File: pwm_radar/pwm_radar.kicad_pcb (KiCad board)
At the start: 2 copper layers, 32.6 x 46.1 mm, 21 parts, among them J1 Conn_Coaxial, J2 Conn_01x01_Pin, J3 Conn_01x01_Pin, J4 Conn_Coaxial, J5 Conn_Coaxial, J6 Conn_Coaxial, J7 Conn_01x01_Pin, J8 Conn_01x01_Pin

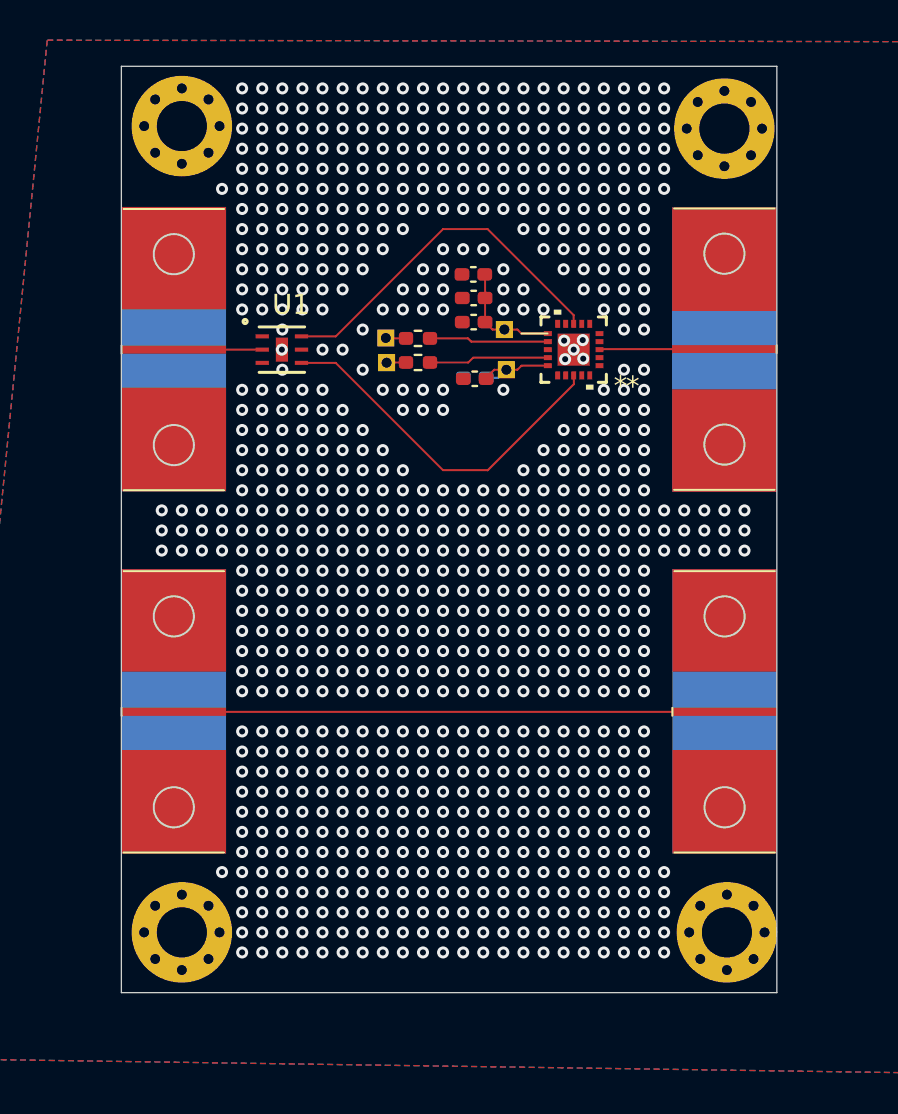
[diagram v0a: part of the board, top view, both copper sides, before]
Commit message: added 50 ohm lines
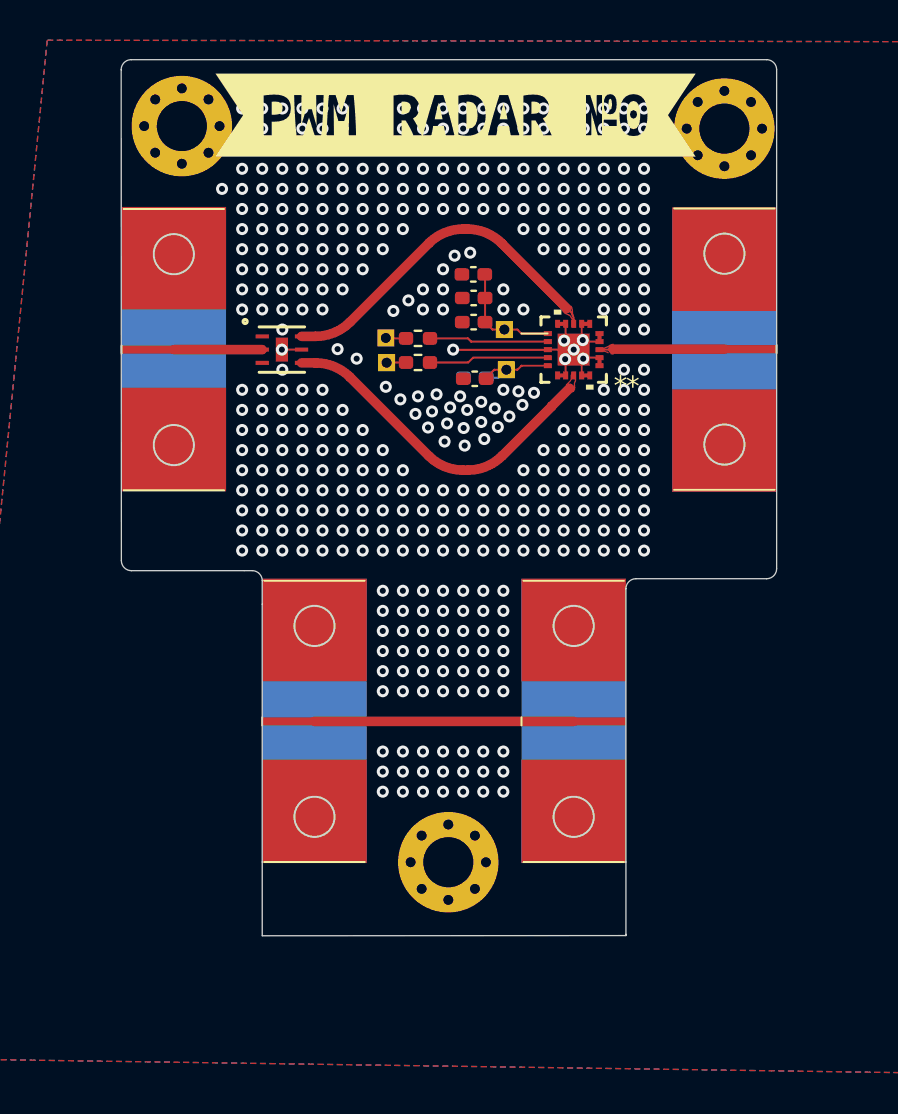
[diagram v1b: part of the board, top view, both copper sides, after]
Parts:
- removed H3: MountingHole_Pad, MountingHole:MountingHole_2.5mm_Pad_Via
- added kibuzzard-6A209544: G***, kibuzzard-6A209544, F.Cu at (126.6, 86.3)
- added kibuzzard-6A209595: G***, kibuzzard-6A209595, B.Cu at (126.4, 86.5)
- moved J5 20.4 mm to (113.1, 116.5)
- moved J4 19.9 mm to (126.0, 116.5)
- moved H4 13.7 mm to (126.3, 123.5)
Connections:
- U2 pad 21: (no net) -> GND
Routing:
- net Net-(J4-In): track 27.4 -> 12.9 mm
- net GND: track 0.00 -> 14.1 mm, vias 825 -> 464
- net RF2: track 18.0 -> 16.9 mm
- net (no net): vias 7 -> 2
- added copper zone on F.Cu, net Net-(J6-In)
- added copper zone on F.Cu, net RF1
- added copper zone on F.Cu, net RF2
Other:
- board size 32.6 x 46.1 mm -> 32.6 x 43.6 mm

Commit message: minor changes
minor changes
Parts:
- moved J4 13.0 mm to (139.0, 116.5), turned to -90 degrees
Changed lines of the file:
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@@
 	(footprint "pwm_radar_lib:Wurth_RF_PWM_Conn"
 		(layer "F.Cu")
-		(at 126 116.5 90)
+		(at 139.005845 116.5 -90)
 		(property "Reference" "J4"
-			(at -9.9 4 90)
+			(at -9.9 4 270)
 			(unlocked yes)
 			(layer "F.SilkS")
@@
 		)
 		(property "Value" "Conn_Coaxial"
-			(at 0 1 90)
+			(at 0 1 270)
 			(unlocked yes)
 			(layer "F.Fab")
@@
 		)
 		(property "Datasheet" ""
-			(at 0 0 90)
+			(at 0 0 270)
 			(unlocked yes)
 			(layer "F.Fab")
@@
 		)
 		(property "Description" "coaxial connector (BNC, SMA, SMB, SMC, Cinch/RCA, LEMO, ...)"
-			(at 0 0 90)
+			(at 0 0 270)
 			(unlocked yes)
 			(layer "F.Fab")
@@
 		(attr smd)
 		(fp_line
-			(start -0.2 3.9)
-			(end 0.2 3.9)
+			(start -7 9)
+			(end -7 4)
 			(stroke
 				(width 0.1)
@@
 		)
 		(fp_line
-			(start -7 9)
-			(end -7 4)
+			(start -0.2 3.9)
+			(end 0.2 3.9)
 			(stroke
 				(width 0.1)
@@
 		)
 		(fp_circle
-			(center 4.75 6.5)
-			(end 4.75 7.5)
+			(center -4.75 6.5)
+			(end -4.75 7.5)
 			(stroke
 				(width 0.1)
@@
 		)
 		(fp_circle
-			(center -4.75 6.5)
-			(end -4.75 7.5)
+			(center 4.75 6.5)
+			(end 4.75 7.5)
 			(stroke
 				(width 0.1)
@@
 		)
 		(fp_text user "${REFERENCE}"
-			(at 0 2.5 90)
+			(at 0 2.5 270)
 			(unlocked yes)
 			(layer "F.Fab")
@@
 		)
 		(pad "1" connect rect
-			(at 0 6.5 90)
+			(at 0 6.5 270)
 			(size 0.4 5.2)
 			(layers "F.Cu" "F.Mask")
@@
 		)
 		(pad "2" connect rect
-			(at -4.475 6.5 90)
+			(at -4.475 6.5 270)
 			(size 5.15 5.2)
 			(layers "F.Cu" "F.Mask")
@@
 		)
 		(pad "2" connect rect
-			(at 0.025 6.5 90)
+			(at 0.025 6.5 270)
 			(size 14.15 5.2)
 			(layers "B.Cu" "B.Mask")
@@
 		)
 		(pad "2" connect rect
-			(at 4.55 6.5 90)
+			(at 4.55 6.5 270)
 			(size 5.1 5.2)
 			(layers "F.Cu" "F.Mask")
@@
 		)
 	)
+	(gr_poly
+		(pts
+			(xy 136.55 98.2) (xy 136.55 97.73) (xy 134.49 97.74) (xy 133.96 97.92) (xy 133.96 98.08) (xy 134.44 98.2)
+		)
+		(stroke
+			(width 0.1)
+			(type solid)
+		)
+		(fill yes)
+		(layer "F.Mask")
+	)
 	(gr_rect
 		(start 110 83.695)
@@
 	)
 	(gr_rect
+		(start 110 109.025)
+		(end 142.61 130.305)
+		(stroke
+			(width 0.1)
+			(type solid)
+		)
+		(fill yes)
+		(layer "F.Mask")
+	)
+	(gr_rect
+		(start 110 123)
+		(end 142.61 130.255)
+		(stroke
+			(width 0.1)
+			(type solid)
+		)
+		(fill yes)
+		(layer "F.Mask")
+	)
+	(gr_rect
 		(start 110.1 105)
 		(end 142.51 109.025)
@@
 		(layer "F.Mask")
 	)
+	(gr_line
+		(start 133.96 97.92)
+		(end 133.96 98.08)
+		(stroke
+			(width 0.1)
+			(type default)
+		)
+		(layer "F.Mask")
+	)
+	(gr_line
+		(start 133.96 98.08)
+		(end 134.44 98.2)
+		(stroke
+			(width 0.1)
+			(type default)
+		)
+		(layer "F.Mask")
+	)
+	(gr_line
+		(start 134.44 98.2)
+		(end 136.55 98.2)
+		(stroke
+			(width 0.1)
+			(type default)
+		)
+		(layer "F.Mask")
+	)
+	(gr_line
+		(start 134.49 97.74)
+		(end 133.96 97.92)
+		(stroke
+			(width 0.1)
+			(type default)
+		)
+		(layer "F.Mask")
+	)
+	(gr_line
+		(start 136.55 97.73)
+		(end 134.49 97.74)
+		(stroke
+			(width 0.1)
+			(type default)
+		)
+		(layer "F.Mask")
+	)
+	(gr_line
+		(start 136.55 98.2)
+		(end 136.55 97.73)
+		(stroke
+			(width 0.1)
+			(type default)
+		)
+		(layer "F.Mask")
+	)
 	(gr_rect
 		(start 136.61 83.645)
@@
 	)
 	(gr_rect
-		(start 109.995 124)
-		(end 142.605 130)
+		(start 110 109)
+		(end 142.61 130.255)
+		(stroke
+			(width 0.1)
+			(type solid)
+		)
+		(fill yes)
+		(layer "B.Mask")
+	)
+	(gr_rect
+		(start 110 123.255)
+		(end 142.61 130.255)
 		(stroke
 			(width 0.1)
@@
 	(gr_rect
 		(start 110.1 105)
-		(end 142.51 109.025)
+		(end 142.51 110.025)
 		(stroke
 			(width 0.1)
@@
 		(layer "B.Mask")
 	)
+	(gr_rect
+		(start 110.1 109.025)
+		(end 142.61 130.255)
+		(stroke
+			(width 0.1)
+			(type solid)
+		)
+		(fill no)
+		(layer "B.Mask")
+	)

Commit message: pcb files changes
pcb changes
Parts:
- added H3: MountingHole_Pad, MountingHole:MountingHole_2.5mm_Pad_Via, F.Cu at (138.4, 127.3)
- moved H4 12.4 mm to (114.4, 126.9)
- moved J4 6.24 mm to (145.2, 116.5)
- moved J5 5.75 mm to (107.3, 116.5)
- moved H2 0.64 mm to (139.6, 86.5)
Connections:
- U2 pad 21: GND -> (no net)
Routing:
- net Net-(J4-In): track 12.9 -> 24.9 mm
- net GND: vias 464 -> 554
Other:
- board size 32.6 x 43.6 mm -> 32.6 x 47.3 mm

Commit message: changes
changes
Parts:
- removed J1, J4, J5: Conn_Coaxial, pwm_radar_lib:Wurth_RF_PWM_Conn
- removed kibuzzard-6A209544: G***, kibuzzard-6A209544
- removed kibuzzard-6A209595: G***, kibuzzard-6A209595
- added C6: 100p, Capacitor_SMD:C_0402_1005Metric_Pad0.74x0.62mm_HandSolder, F.Cu at (199.0, 65.3)
- C4, J2, J3, J7, J8: moved to F.Cu
- moved U1 107.7 mm to (211.6, 44.7)
- moved H4 100.8 mm to (194.1, 65.2)
- moved U2 99.5 mm to (216.4, 44.7)
- moved J2 92.9 mm to (199.1, 43.8), turned to 0 degrees
- moved H1 91.1 mm to (194.1, 45.5)
- moved J7 90.2 mm to (199.1, 49.9), turned to 0 degrees
- moved H3 88.5 mm to (194.1, 58.6)
- moved R1 88.2 mm to (202.3, 55.5), turned to 0 degrees
- moved R2 87.8 mm to (202.3, 57.5), turned to 0 degrees
- moved J6 87.4 mm to (223.0, 55.7)
- moved J3 86.1 mm to (199.1, 46.9), turned to 0 degrees
- moved J8 83.7 mm to (199.1, 53.0), turned to 0 degrees
- moved C1 82.5 mm to (199.0, 55.5), turned to 0 degrees
- moved C2 81.0 mm to (199.0, 57.4), turned to 0 degrees
- moved C4 80.9 mm to (199.0, 61.4), turned to 0 degrees
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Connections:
- J6 pad 1: Net-(J6-In) -> (no net)
- J6 pad 2: GND -> (no net)
- U1 pad 1: GND -> (no net)
- U1 pad 2: Net-(J1-In) -> (no net)
- U1 pad 3: GND -> (no net)
- U1 pad 4: RF2 -> (no net)
- U1 pad 5: GND -> (no net)
- U1 pad 6: RF1 -> (no net)
- U1 pad 7: GND -> (no net)
- U2 pad 1: GND -> (no net)
- U2 pad 10: GND -> (no net)
- U2 pad 11: VDD -> (no net)
- U2 pad 12: CTRL -> (no net)
- U2 pad 13: GND -> (no net)
- U2 pad 14: EN -> (no net)
- U2 pad 15: VSS -> (no net)
- U2 pad 16: GND -> (no net)
- U2 pad 17: GND -> (no net)
- U2 pad 18: RF2 -> (no net)
- U2 pad 19: GND -> (no net)
- U2 pad 2: GND -> (no net)
- U2 pad 20: GND -> (no net)
- U2 pad 3: Net-(J6-In) -> (no net)
- U2 pad 4: GND -> (no net)
- U2 pad 5: GND -> (no net)
- U2 pad 6: GND -> (no net)
- U2 pad 7: GND -> (no net)
- U2 pad 8: RF1 -> (no net)
- U2 pad 9: GND -> (no net)
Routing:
- net Net-(J4-In): track 24.9 -> 0.00 mm
- net RF1: track 17.6 -> 0.00 mm
- net RF2: track 16.9 -> 0.00 mm
- net GND: track 14.1 -> 0.00 mm, vias 554 -> 0
- net Net-(J6-In): track 6.26 -> 0.00 mm
- net EN: track 5.96 -> 0.00 mm
- net CTRL: track 5.93 -> 0.00 mm
- net VDD: track 5.74 -> 0.00 mm
- net VSS: track 4.53 -> 0.00 mm
- net Net-(J1-In): track 4.40 -> 0.00 mm
- net Net-(J7-Pin_1): track 1.02 -> 0.00 mm
- net Net-(J2-Pin_1): track 1.00 -> 0.00 mm
- net (no net): vias 2 -> 0
- removed copper zone on B.Cu, net GND
- removed copper zone on F.Cu, net GND
- removed copper zone on F.Cu, net Net-(J6-In)
- removed copper zone on F.Cu, net RF1
- removed copper zone on F.Cu, net RF2
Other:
- board size 32.6 x 47.3 mm -> 2 x 11.5 mm

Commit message: pcb changes
pcb changes
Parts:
- added J1: Conn_Coaxial, pwm_radar_lib:Wurth_RF_PWM_Conn, F.Cu at (83.6, 57.0)
- added J4: Conn_Coaxial, pwm_radar_lib:Wurth_RF_PWM_Conn, F.Cu at (130.0, 76.0)
- added J5: Conn_Coaxial, pwm_radar_lib:Wurth_RF_PWM_Conn, F.Cu at (83.0, 76.0)
- C1, C2, C3, C4, C5, C6, J2, J3, J7, J8: moved to B.Cu
- moved U1 114.3 mm to (98.0, 57.0)
- moved J6 106.5 mm to (116.5, 57.0), turned to 90 degrees
- moved U2 103.2 mm to (114.0, 57.0)
- moved J2 95.0 mm to (104.9, 56.7), turned to 180 degrees
- moved R1 94.9 mm to (107.4, 56.6), turned to 180 degrees
- moved R2 92.1 mm to (110.1, 57.8), turned to 180 degrees
- moved J7 92.1 mm to (107.4, 58.4), turned to 180 degrees
- moved C4 91.6 mm to (107.4, 60.0), turned to 180 degrees
- moved C6 91.6 mm to (107.5, 62.4), turned to 180 degrees
- moved C5 91.6 mm to (107.5, 61.2), turned to 180 degrees
- moved C3 91.1 mm to (108.0, 55.7), turned to 180 degrees
- moved C2 91.1 mm to (108.0, 54.6), turned to 180 degrees
- moved C1 91.0 mm to (108.0, 53.5), turned to 180 degrees
- moved J3 89.6 mm to (109.9, 55.6), turned to 180 degrees
- moved J8 89.5 mm to (109.8, 60.0), turned to 180 degrees
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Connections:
- J6 pad 1: (no net) -> Net-(J6-In)
- J6 pad 2: (no net) -> GND
- U1 pad 1: (no net) -> GND
- U1 pad 2: (no net) -> Net-(J1-In)
- U1 pad 3: (no net) -> GND
- U1 pad 4: (no net) -> RF1-
- U1 pad 5: (no net) -> GND
- U1 pad 6: (no net) -> RF1+
- U1 pad 7: (no net) -> GND
- U2 pad 1: (no net) -> GND
- U2 pad 10: (no net) -> GND
- U2 pad 11: (no net) -> VDD
- U2 pad 12: (no net) -> CTRL
- U2 pad 13: (no net) -> GND
- U2 pad 14: (no net) -> EN
- U2 pad 15: (no net) -> VSS
- U2 pad 16: (no net) -> GND
- U2 pad 17: (no net) -> GND
- U2 pad 18: (no net) -> RF1-
- U2 pad 19: (no net) -> GND
- U2 pad 2: (no net) -> GND
- U2 pad 20: (no net) -> GND
- U2 pad 21: (no net) -> GND
- U2 pad 3: (no net) -> Net-(J6-In)
- U2 pad 4: (no net) -> GND
- U2 pad 5: (no net) -> GND
- U2 pad 6: (no net) -> GND
- U2 pad 7: (no net) -> GND
- U2 pad 8: (no net) -> RF1+
- U2 pad 9: (no net) -> GND
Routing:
- net Net-(J4-In): track 0.00 -> 38.0 mm
- net RF1+: track 0.00 -> 19.8 mm
- net RF1-: track 0.00 -> 19.8 mm
- net Net-(J6-In): track 0.00 -> 8.81 mm
- net VSS: track 0.00 -> 8.46 mm
- net Net-(J1-In): track 0.00 -> 7.95 mm
- net VDD: track 0.00 -> 6.58 mm
- net GND: track 0.00 -> 6.12 mm, vias 0 -> 417
- net CTRL: track 0.00 -> 4.75 mm
- net Net-(J7-Pin_1): track 0.00 -> 2.39 mm
- net EN: track 0.00 -> 2.13 mm
- net Net-(J2-Pin_1): track 0.00 -> 1.92 mm
- added copper zone on B.Cu, net GND
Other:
- board size 2 x 11.5 mm -> 39 x 39 mm

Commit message: vivaldi antenna put in
vivaldi antenna put in
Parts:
- removed H1, H2, H3, H4: MountingHole_Pad, MountingHole:MountingHole_2.5mm_Pad_Via
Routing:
- net GND: vias 417 -> 416
